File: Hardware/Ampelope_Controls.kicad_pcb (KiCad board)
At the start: 2 copper layers, 71 x 110 mm, 34 parts, among them J10 Audio1_Out, J11 Audio2_Out, J12 Audio3_Out, J13 Audio4_Out, J14 Env1_Out, J15 Env2_Out, J16 Env3_Out, J17 Env4_Out, J2 Gate1_In, J3 Gate2_In, J4 Gate3_In, J5 Gate4_In, J6 Audio1_In, J7 Audio2_In, J8 Audio3_In, J9 Audio4_In

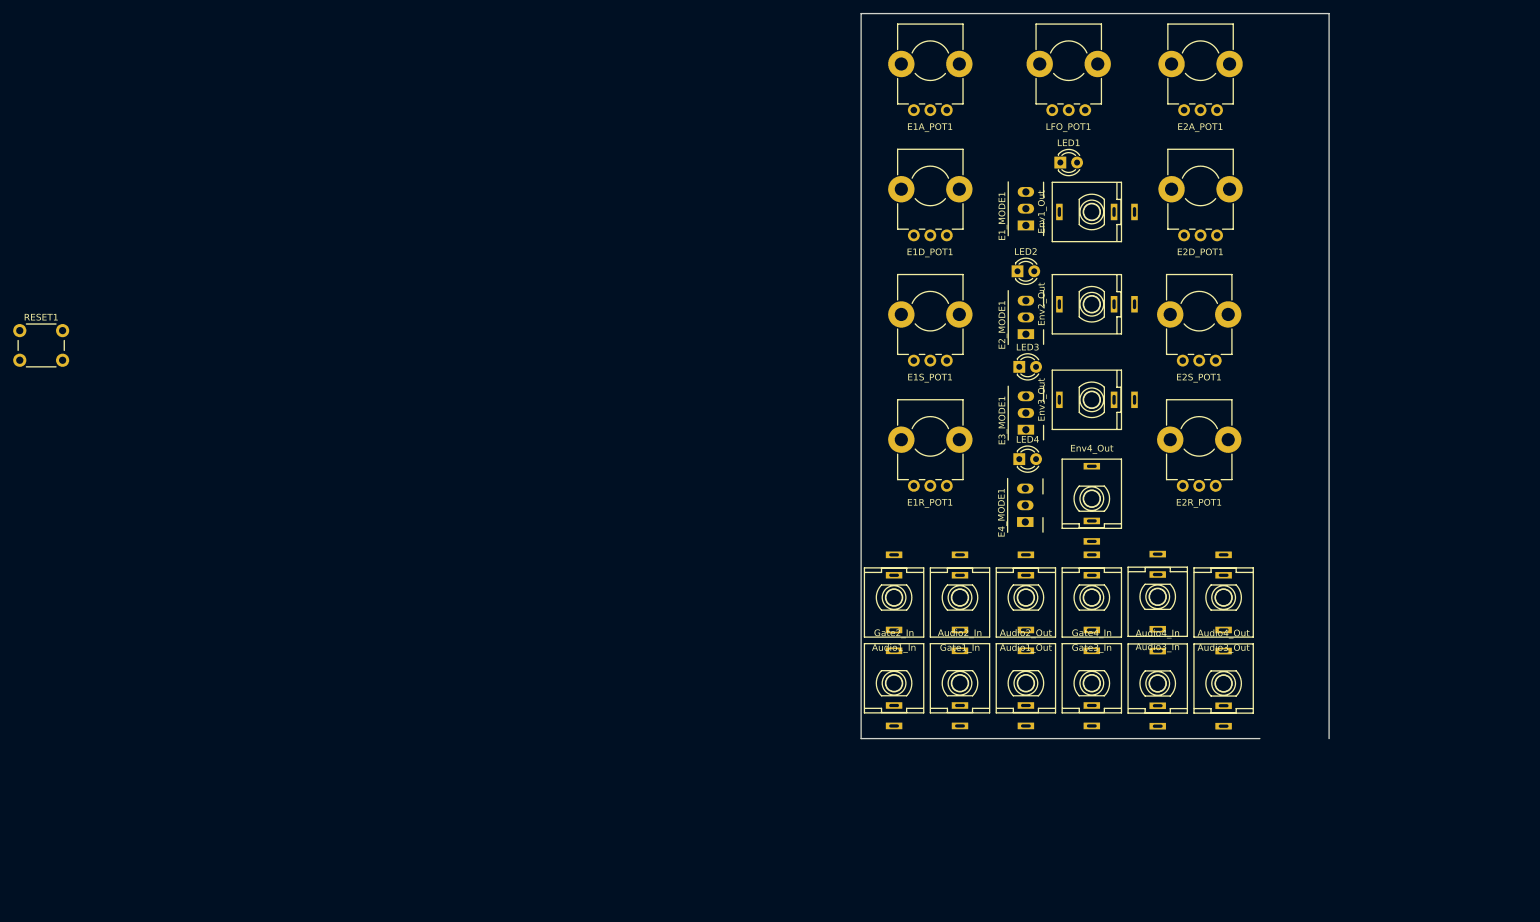
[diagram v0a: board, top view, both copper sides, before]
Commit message: First Draft Layout of controls PCB
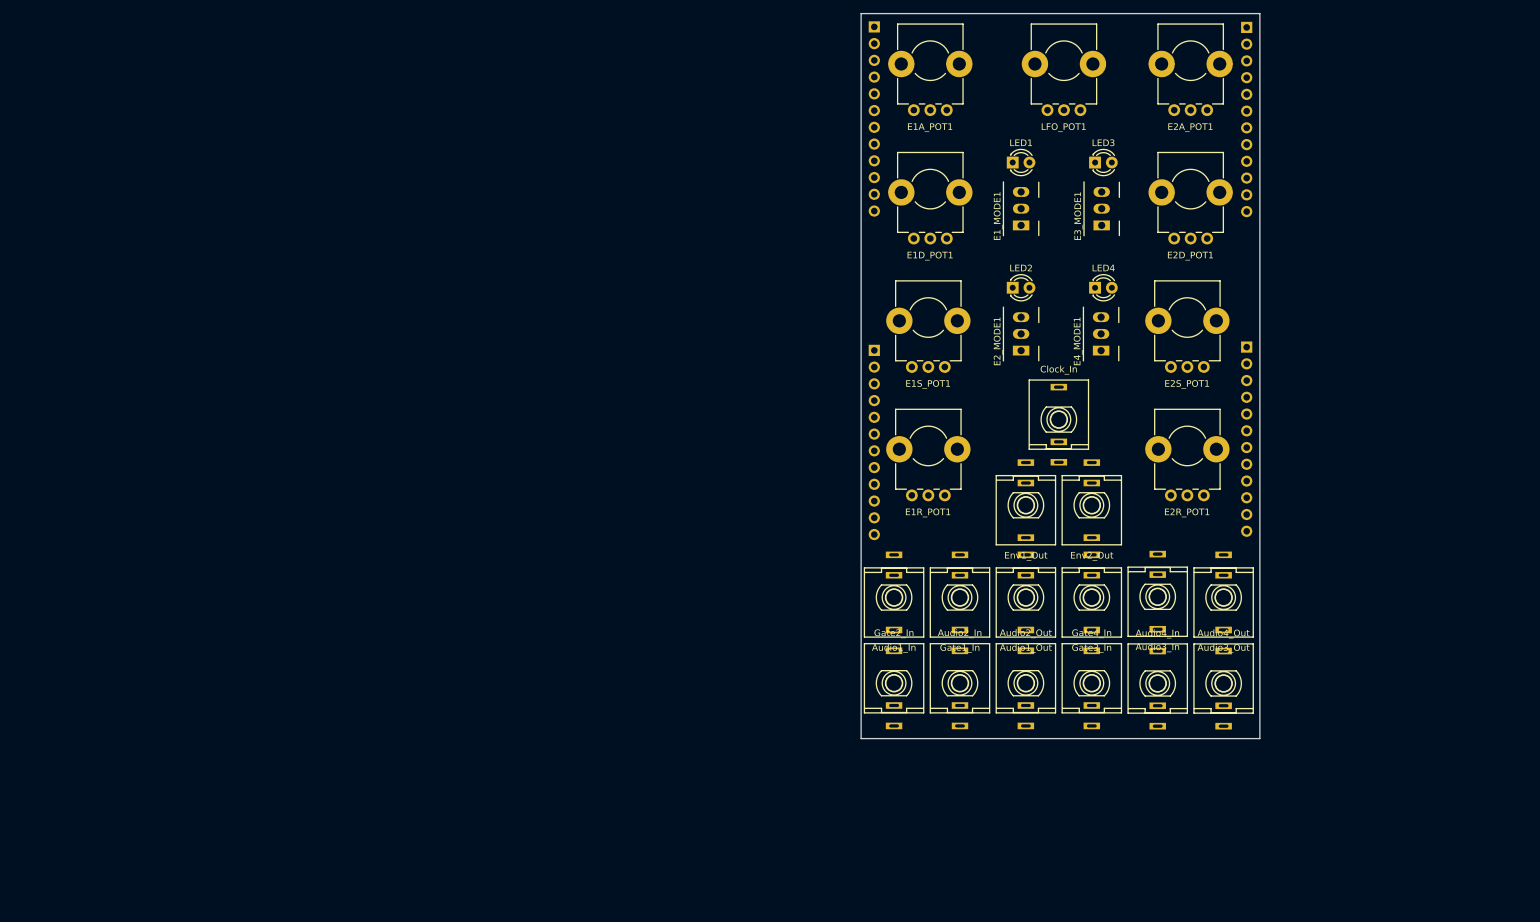
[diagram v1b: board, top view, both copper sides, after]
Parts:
- removed RESET1: SW_Push, Custom_Footprints:SW_PUSH_6mm_aligned
- added J1: Clock_In, Custom_Footprints:THONKICONN_hole, F.Cu at (90.0, 87.0)
- added J18: Conn_01x12_Male, Connector_PinHeader_2.54mm:PinHeader_1x12_P2.54mm_Vertical, B.Cu at (118.5, 27.5)
- added J19: Conn_01x12_Male, Connector_PinHeader_2.54mm:PinHeader_1x12_P2.54mm_Vertical, B.Cu at (118.5, 76.0)
- J16: value Env3_Out -> Conn_01x12_Male; footprint Custom_Footprints:THONKICONN_hole -> Connector_PinHeader_2.54mm:PinHeader_1x12_P2.54mm_Vertical; moved to B.Cu
- J17: value Env4_Out -> Conn_01x12_Male; footprint Custom_Footprints:THONKICONN_hole -> Connector_PinHeader_2.54mm:PinHeader_1x12_P2.54mm_Vertical; moved to B.Cu
- moved J17 78.8 mm to (62.0, 27.4), turned to 180 degrees
- moved J14 45.6 mm to (85.0, 100.0), turned to 180 degrees
- moved J16 33.8 mm to (62.0, 76.5), turned to 180 degrees
- moved E3_MODE1 33.1 mm to (96.5, 55.0)
- moved LED3 33.1 mm to (95.5, 48.0)
- moved J15 30.5 mm to (95.0, 100.0), turned to 180 degrees
- moved E4_MODE1 28.4 mm to (96.4, 74.0)
- moved LED4 28.4 mm to (95.5, 67.0)
- moved LED1 7.22 mm to (83.0, 48.0)
- moved E2_MODE1 2.60 mm to (84.3, 74.0)
- moved LED2 2.60 mm to (83.0, 67.0)
- moved E2R_POT1 2.31 mm to (109.5, 91.0)
- moved E2S_POT1 2.04 mm to (109.5, 71.5)
- moved E2D_POT1 1.58 mm to (110.0, 52.0)
- moved E2A_POT1 1.50 mm to (110.0, 32.5)
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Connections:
- J14 pad 3: /Led1_Out -> /Env1_Out
- J15 pad 3: /Led2_Out -> /Env2_Out
- J16 pad 1: GND -> /Gate1_In
- J16 pad 2: unconnected-(J16-Pad2) -> /Gate2_In
- J16 pad 3: /Led3_Out -> /Gate3_In
- J17 pad 1: GND -> /LFO_Speed
- J17 pad 2: unconnected-(J17-Pad2) -> /EnvB_Attack
- J17 pad 3: /Led4_Out -> /EnvB_Decay
- LED1 pad 2: /Env1_Out -> /Led1_Out
- LED2 pad 2: /Env2_Out -> /Led2_Out
- LED3 pad 2: /Env3_Out -> /Led3_Out
- LED4 pad 2: /Env4_Out -> /Led4_Out
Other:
- board size 71 x 110 mm -> 60.5 x 110 mm

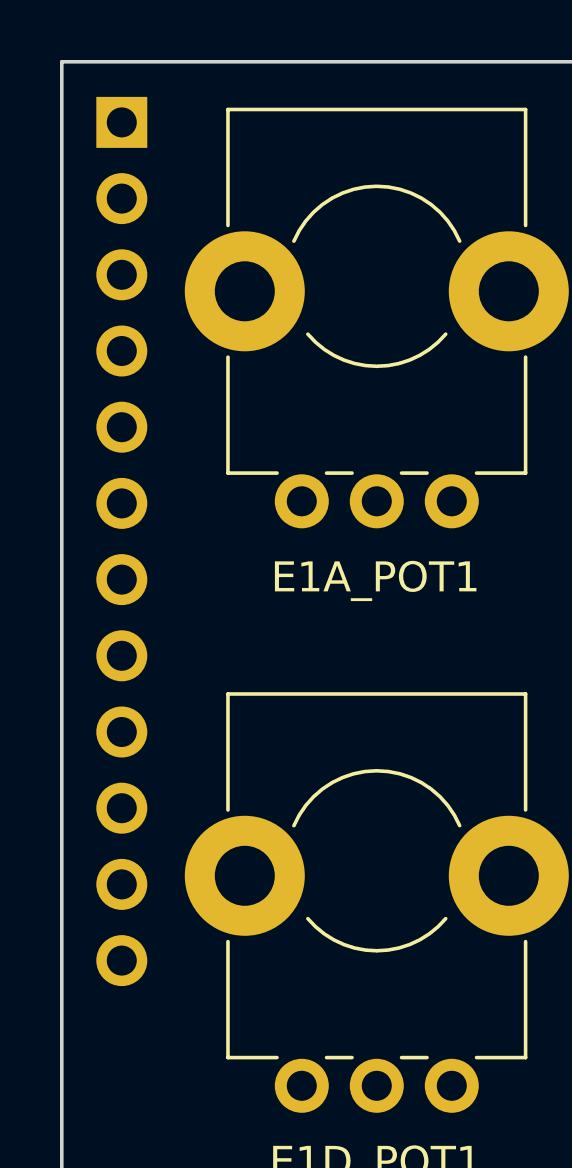
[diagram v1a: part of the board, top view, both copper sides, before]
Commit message: Started rough placement of component board
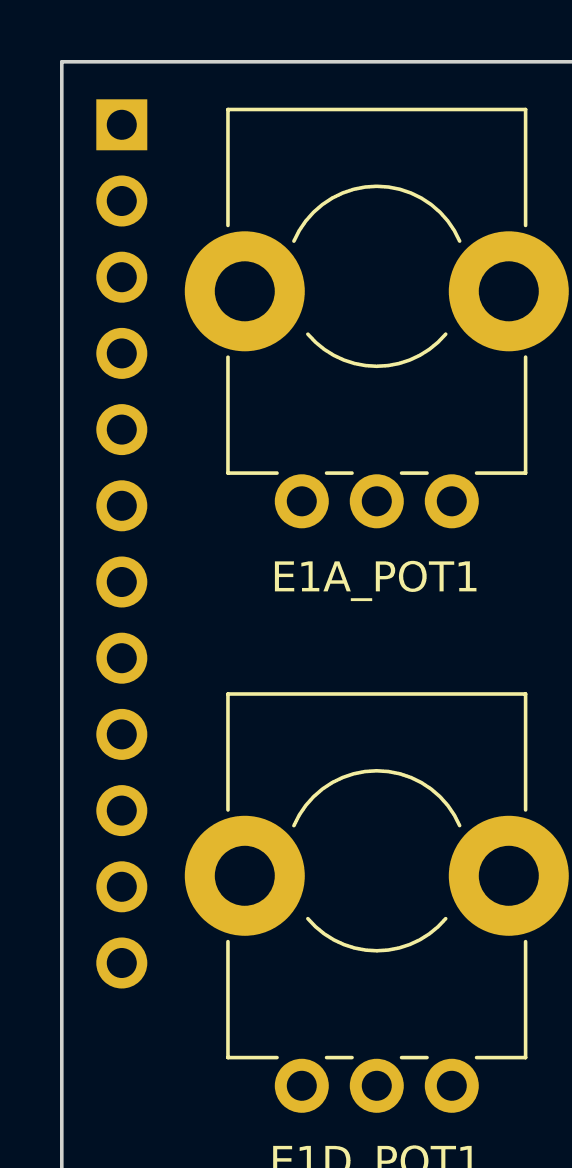
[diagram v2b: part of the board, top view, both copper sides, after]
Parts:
- moved J3 0.08 mm to (62.0, 27.5)
- renumbered J18 to J1, J7 to J10, J8 to J11, J9 to J12, J10 to J13, J11 to J14, J12 to J15, J13 to J16, J1 to J17, J14 to J18, J15 to J19, J19 to J2, J17 to J3, J16 to J4, J2 to J5, J3 to J6, J4 to J7, J5 to J8, J6 to J9

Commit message: Work on panel and control layout
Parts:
- moved J19 50.5 mm to (139.1, 124.6)
- moved J17 48.4 mm to (130.3, 113.8)
- moved E2S_POT1 47.8 mm to (150.5, 96.1)
- moved E2R_POT1 47.8 mm to (150.5, 115.5)
- moved J10 47.7 mm to (115.2, 152.6), turned to 180 degrees
- moved J14 47.7 mm to (125.2, 152.6), turned to 180 degrees
- moved J6 47.7 mm to (105.2, 152.6), turned to 180 degrees
- moved J8 47.7 mm to (135.2, 152.6), turned to 180 degrees
- moved J12 47.6 mm to (145.2, 152.6), turned to 180 degrees
- moved J16 47.6 mm to (155.2, 152.6), turned to 180 degrees
- moved E2A_POT1 47.5 mm to (150.5, 57.3)
- moved E2D_POT1 47.4 mm to (150.5, 76.7)
- moved J11 47.2 mm to (145.2, 138.6)
- moved J9 47.2 mm to (105.2, 138.7)
- moved J13 47.1 mm to (125.2, 138.6)
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
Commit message: First draft of panel and control boards complete
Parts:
- LED1, LED2, LED3, LED4: footprint LED_THT:LED_D3.0mm -> Custom_Footprints:LED_D3.0mm
- moved J13 20.0 mm to (105.2, 138.7)
- moved J14 20.0 mm to (105.2, 152.6)
- moved J6 20.0 mm to (125.2, 152.6)
- moved LED4 16.4 mm to (141.7, 106.4)
- moved LED2 15.6 mm to (118.9, 106.4)
- moved J5 10.0 mm to (125.2, 138.6)
- moved J9 10.0 mm to (115.2, 138.7)
- moved LED3 6.79 mm to (141.7, 68.1)
- moved LED1 4.54 mm to (118.9, 68.1)
- moved LFO_POT1 4.10 mm to (130.3, 61.4)
- moved E2_MODE1 3.00 mm to (123.9, 95.2)
- moved E4_MODE1 3.00 mm to (136.7, 95.2)
- moved J18 2.39 mm to (120.2, 126.6), turned to -90 degrees
- moved J19 2.33 mm to (140.3, 126.6), turned to 90 degrees
- moved J17 1.70 mm to (130.3, 115.5)
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
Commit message: Layout on component board
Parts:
- J19: value Env2_Out -> Env3_Out
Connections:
- J19 pad 3: /Env2_Out -> /Env3_Out
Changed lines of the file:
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@@
     (pad "0" np_thru_hole circle locked (at 4.4 0.5 90) (size 4 4) (drill 2) (layers *.Cu *.Mask))
     (pad "1" thru_hole circle locked (at 2.5 7.5 90) (size 1.8 1.8) (drill 1) (layers *.Cu *.Mask)
-      (net 34 "+3.3VA") (pinfunction "1"))
+      (net 34 "+3.3VA") (pinfunction "1") (pintype "passive"))
     (pad "2" thru_hole circle locked (at 0 7.5 90) (size 1.8 1.8) (drill 1) (layers *.Cu *.Mask)
-      (net 55 "/EnvB_Sustain") (pinfunction "2"))
+      (net 55 "/EnvB_Sustain") (pinfunction "2") (pintype "passive"))
     (pad "3" thru_hole circle locked (at -2.5 7.5 90) (size 1.8 1.8) (drill 1) (layers *.Cu *.Mask)
-      (net 1 "GND") (pinfunction "3"))
+      (net 1 "GND") (pinfunction "3") (pintype "passive"))
     (model "D:/docs/kiCad/Custom_Footprints.pretty/3dmodels/ALPHA-RD901F-40.step"
       (offset (xyz -0 -0.2 0))
@@
     (pad "0" np_thru_hole circle locked (at 4.4 0.5 90) (size 4 4) (drill 2) (layers *.Cu *.Mask))
     (pad "1" thru_hole circle locked (at 2.5 7.5 90) (size 1.8 1.8) (drill 1) (layers *.Cu *.Mask)
-      (net 34 "+3.3VA") (pinfunction "1"))
+      (net 34 "+3.3VA") (pinfunction "1") (pintype "passive"))
     (pad "2" thru_hole circle locked (at 0 7.5 90) (size 1.8 1.8) (drill 1) (layers *.Cu *.Mask)
-      (net 54 "/EnvB_Release") (pinfunction "2"))
+      (net 54 "/EnvB_Release") (pinfunction "2") (pintype "passive"))
     (pad "3" thru_hole circle locked (at -2.5 7.5 90) (size 1.8 1.8) (drill 1) (layers *.Cu *.Mask)
-      (net 1 "GND") (pinfunction "3"))
+      (net 1 "GND") (pinfunction "3") (pintype "passive"))
     (model "D:/docs/kiCad/Custom_Footprints.pretty/3dmodels/ALPHA-RD901F-40.step"
       (offset (xyz -0 -0.2 0))
@@
     (fp_circle (center 0 0) (end 1.5 0) (layer "F.Fab") (width 0.1) (fill none))
     (pad "1" thru_hole rect locked (at -1.27 0) (size 1.8 1.8) (drill 0.9) (layers *.Cu *.Mask)
-      (net 1 "GND") (pinfunction "K"))
+      (net 1 "GND") (pinfunction "K") (pintype "passive"))
     (pad "2" thru_hole circle locked (at 1.27 0) (size 1.8 1.8) (drill 0.9) (layers *.Cu *.Mask)
-      (net 20 "/Led2_Out") (pinfunction "A"))
+      (net 20 "/Led2_Out") (pinfunction "A") (pintype "passive"))
     (model "${KICAD6_3DMODEL_DIR}/LED_THT.3dshapes/LED_D3.0mm.wrl"
       (offset (xyz -1.3 0 0))
@@
     (fp_circle (center 0 0) (end 1.5 0) (layer "F.Fab") (width 0.1) (fill none))
     (pad "1" thru_hole rect locked (at -1.27 0) (size 1.8 1.8) (drill 0.9) (layers *.Cu *.Mask)
-      (net 1 "GND") (pinfunction "K"))
+      (net 1 "GND") (pinfunction "K") (pintype "passive"))
     (pad "2" thru_hole circle locked (at 1.27 0) (size 1.8 1.8) (drill 0.9) (layers *.Cu *.Mask)
-      (net 16 "/Led1_Out") (pinfunction "A"))
+      (net 16 "/Led1_Out") (pinfunction "A") (pintype "passive"))
     (model "${KICAD6_3DMODEL_DIR}/LED_THT.3dshapes/LED_D3.0mm.wrl"
       (offset (xyz -1.3 0 0))
@@
       (effects (font (size 1 1) (thickness 0.15)))
     )
-    (fp_text value "Env2_Out" (at 0 -7.62 90) (layer "F.SilkS")
+    (fp_text value "Env3_Out" (at 0 -7.62 90) (layer "F.SilkS")
       (effects (font (size 1 1) (thickness 0.15)))
     )
@@
       (net 47 "unconnected-(J19-Pad2)") (pintype "passive+no_connect"))
     (pad "3" thru_hole rect locked (at 0 -4.92 90) (size 2.5 1) (drill oval 1.5 0.5) (layers *.Cu *.Mask "F.SilkS")
-      (net 24 "/Env2_Out") (pintype "passive"))
+      (net 32 "/Env3_Out") (pintype "passive"))
     (model ":custom_3d:PJ301M-12 Thonkiconn v0.2.stp"
       (offset (xyz 0 0.6 0))
@@
     (pad "0" np_thru_hole circle locked (at -4.4 0.5 90) (size 4 4) (drill 2) (layers *.Cu *.Mask))
     (pad "1" thru_hole circle locked (at 2.5 7.5 90) (size 1.8 1.8) (drill 1) (layers *.Cu *.Mask)
-      (net 34 "+3.3VA") (pinfunction "1"))
+      (net 34 "+3.3VA") (pinfunction "1") (pintype "passive"))
     (pad "2" thru_hole circle locked (at 0 7.5 90) (size 1.8 1.8) (drill 1) (layers *.Cu *.Mask)
-      (net 50 "/EnvA_Release") (pinfunction "2"))
+      (net 50 "/EnvA_Release") (pinfunction "2") (pintype "passive"))
     (pad "3" thru_hole circle locked (at -2.5 7.5 90) (size 1.8 1.8) (drill 1) (layers *.Cu *.Mask)
-      (net 1 "GND") (pinfunction "3"))
+      (net 1 "GND") (pinfunction "3") (pintype "passive"))
     (model "D:/docs/kiCad/Custom_Footprints.pretty/3dmodels/ALPHA-RD901F-40.step"
       (offset (xyz -0 -0.2 0))
@@
     (pad "0" np_thru_hole circle locked (at 4.4 0.5 90) (size 4 4) (drill 2) (layers *.Cu *.Mask))
     (pad "1" thru_hole circle locked (at 2.5 7.5 90) (size 1.8 1.8) (drill 1) (layers *.Cu *.Mask)
-      (net 34 "+3.3VA") (pinfunction "1"))
+      (net 34 "+3.3VA") (pinfunction "1") (pintype "passive"))
     (pad "2" thru_hole circle locked (at 0 7.5 90) (size 1.8 1.8) (drill 1) (layers *.Cu *.Mask)
-      (net 53 "/EnvB_Decay") (pinfunction "2"))
+      (net 53 "/EnvB_Decay") (pinfunction "2") (pintype "passive"))
     (pad "3" thru_hole circle locked (at -2.5 7.5 90) (size 1.8 1.8) (drill 1) (layers *.Cu *.Mask)
-      (net 1 "GND") (pinfunction "3"))
+      (net 1 "GND") (pinfunction "3") (pintype "passive"))
     (model "D:/docs/kiCad/Custom_Footprints.pretty/3dmodels/ALPHA-RD901F-40.step"
       (offset (xyz -0 -0.2 0))
@@
     (fp_line (start 4.064 -2.54) (end 4.064 2.54) (layer "F.Fab") (width 0.1))
     (pad "1" thru_hole rect locked (at -2.54 0 90) (size 1.5 2.5) (drill 1.0922) (layers *.Cu *.Mask)
-      (net 40 "/Env3_Short") (pinfunction "1"))
+      (net 40 "/Env3_Short") (pinfunction "1") (pintype "passive"))
     (pad "2" thru_hole oval locked (at 0 0 90) (size 1.5 2.5) (drill 1.0922) (layers *.Cu *.Mask)
-      (net 1 "GND") (pinfunction "2"))
+      (net 1 "GND") (pinfunction "2") (pintype "passive"))
     (pad "3" thru_hole oval locked (at 2.54 0 90) (size 1.5 2.5) (drill 1.0922) (layers *.Cu *.Mask)
-      (net 41 "/Env3_LFO") (pinfunction "3"))
+      (net 41 "/Env3_LFO") (pinfunction "3") (pintype "passive"))
     (model "D:/docs/kiCad/Custom_Footprints.pretty/3dmodels/Toggle Switch Daily Well 1AS1T2B4M2QE.STEP"
       (offset (xyz 0 0 8))
@@
     (fp_circle (center 0 0) (end 1.5 0) (layer "F.Fab") (width 0.1) (fill none))
     (pad "1" thru_hole rect locked (at -1.27 0) (size 1.8 1.8) (drill 0.9) (layers *.Cu *.Mask)
-      (net 1 "GND") (pinfunction "K"))
+      (net 1 "GND") (pinfunction "K") (pintype "passive"))
     (pad "2" thru_hole circle locked (at 1.27 0) (size 1.8 1.8) (drill 0.9) (layers *.Cu *.Mask)
-      (net 21 "/Led3_Out") (pinfunction "A"))
+      (net 21 "/Led3_Out") (pinfunction "A") (pintype "passive"))
     (model "${KICAD6_3DMODEL_DIR}/LED_THT.3dshapes/LED_D3.0mm.wrl"
       (offset (xyz -1.3 0 0))
@@
     (fp_line (start -4.064 -2.54) (end -4.064 2.54) (layer "F.Fab") (width 0.1))
     (pad "1" thru_hole rect locked (at -2.54 0 90) (size 1.5 2.5) (drill 1.0922) (layers *.Cu *.Mask)
-      (net 42 "/Env4_Short") (pinfunction "1"))
+      (net 42 "/Env4_Short") (pinfunction "1") (pintype "passive"))
     (pad "2" thru_hole oval locked (at 0 0 90) (size 1.5 2.5) (drill 1.0922) (layers *.Cu *.Mask)
-      (net 1 "GND") (pinfunction "2"))
+      (net 1 "GND") (pinfunction "2") (pintype "passive"))
     (pad "3" thru_hole oval locked (at 2.54 0 90) (size 1.5 2.5) (drill 1.0922) (layers *.Cu *.Mask)
-      (net 43 "/Env4_LFO") (pinfunction "3"))
+      (net 43 "/Env4_LFO") (pinfunction "3") (pintype "passive"))
     (model "D:/docs/kiCad/Custom_Footprints.pretty/3dmodels/Toggle Switch Daily Well 1AS1T2B4M2QE.STEP"
       (offset (xyz 0 0 8))
@@
     (pad "0" np_thru_hole circle locked (at -4.4 0.5 90) (size 4 4) (drill 2) (layers *.Cu *.Mask))
     (pad "1" thru_hole circle locked (at 2.5 7.5 90) (size 1.8 1.8) (drill 1) (layers *.Cu *.Mask)
-      (net 34 "+3.3VA") (pinfunction "1"))
+      (net 34 "+3.3VA") (pinfunction "1") (pintype "passive"))
     (pad "2" thru_hole circle locked (at 0 7.5 90) (size 1.8 1.8) (drill 1) (layers *.Cu *.Mask)
-      (net 52 "/EnvB_Attack") (pinfunction "2"))
+      (net 52 "/EnvB_Attack") (pinfunction "2") (pintype "passive"))
     (pad "3" thru_hole circle locked (at -2.5 7.5 90) (size 1.8 1.8) (drill 1) (layers *.Cu *.Mask)
-      (net 1 "GND") (pinfunction "3"))
+      (net 1 "GND") (pinfunction "3") (pintype "passive"))
     (model "D:/docs/kiCad/Custom_Footprints.pretty/3dmodels/ALPHA-RD901F-40.step"
       (offset (xyz -0 -0.2 0))
@@
     (fp_circle (center 0 0) (end 1.5 0) (layer "F.Fab") (width 0.1) (fill none))
     (pad "1" thru_hole rect locked (at -1.27 0) (size 1.8 1.8) (drill 0.9) (layers *.Cu *.Mask)
-      (net 1 "GND") (pinfunction "K"))
+      (net 1 "GND") (pinfunction "K") (pintype "passive"))
     (pad "2" thru_hole circle locked (at 1.27 0) (size 1.8 1.8) (drill 0.9) (layers *.Cu *.Mask)
-      (net 22 "/Led4_Out") (pinfunction "A"))
+      (net 22 "/Led4_Out") (pinfunction "A") (pintype "passive"))
     (model "${KICAD6_3DMODEL_DIR}/LED_THT.3dshapes/LED_D3.0mm.wrl"
       (offset (xyz -1.3 0 0))
